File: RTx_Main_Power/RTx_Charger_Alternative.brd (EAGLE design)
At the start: 102.9 x 43.2 mm, 11 parts, among them IC1 TL331, Q1 STW11NM80

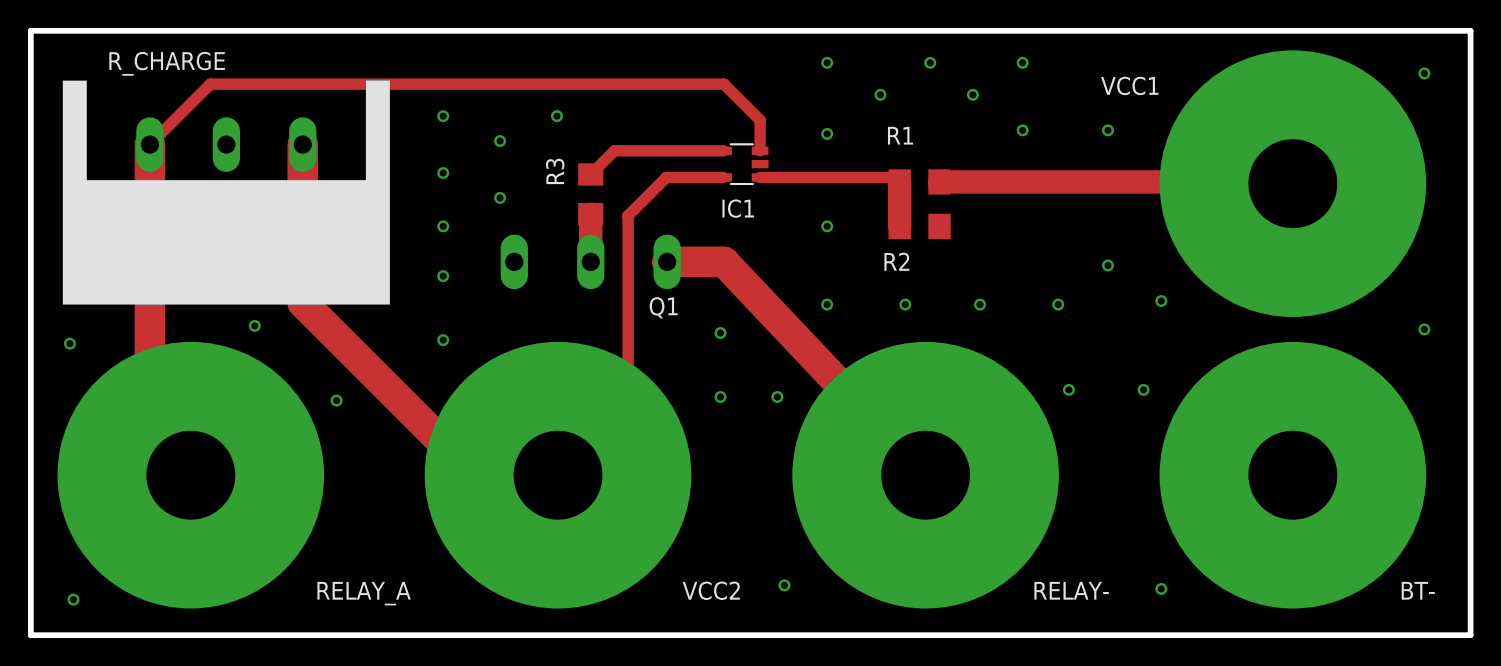
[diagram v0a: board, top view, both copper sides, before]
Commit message: High speed signal routing information added to schematic. Updated Precharge board.
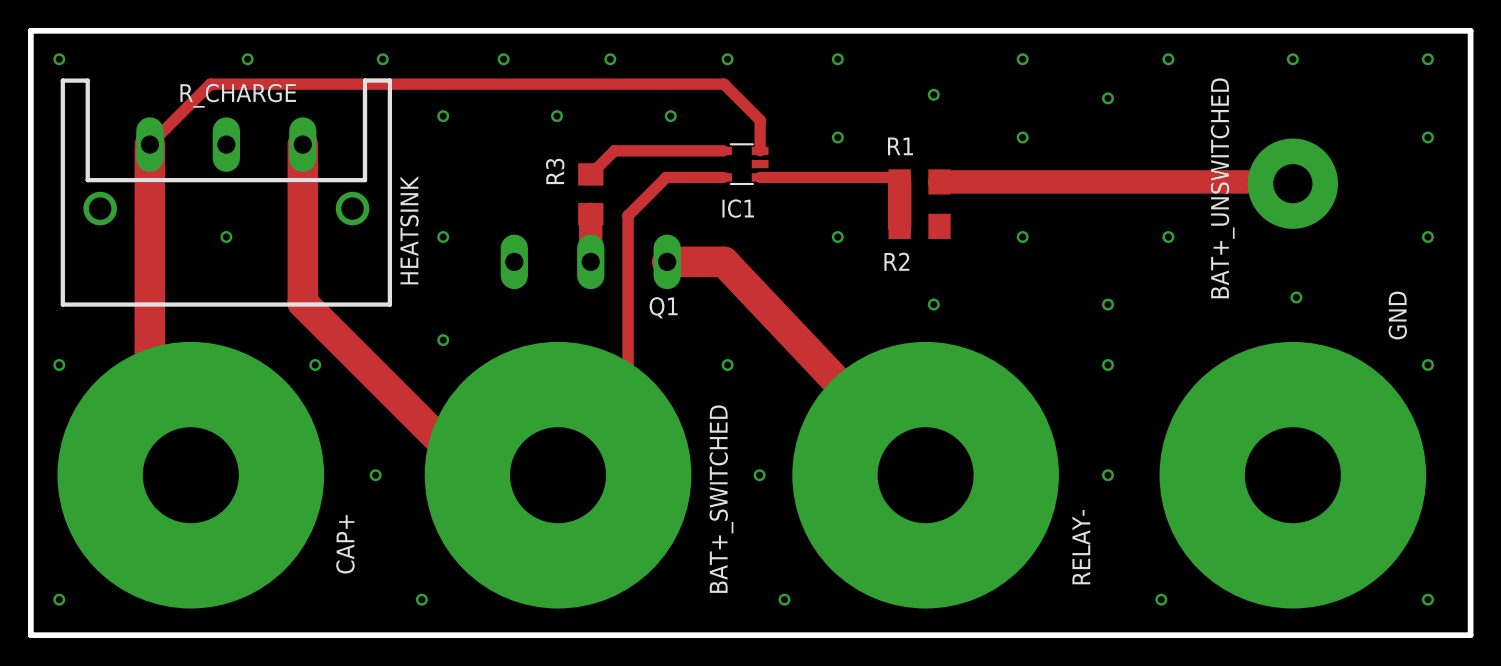
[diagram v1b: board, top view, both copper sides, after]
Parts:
- removed VCC1: TERMINAL, temp_library:TERMINAL_BATTERY
- added BAT+_UNSWITCHED: TERMINAL, temp_library:TERMINAL_RELAY
- added HEATSINK: WA-T247-101E, temp_library:WA-T247-101E
- R_CHARGE: device temp_library:WA-T247-101E -> temp_library:TEH70
- renumbered BT- to GND, RELAY_A to CAP+, VCC2 to BAT+_SWITCHED
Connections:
- net RELAY_A renamed CAP+
- net VCC2 renamed BAT+_SWITCHED
- removed net VCC1: R1.2, VCC1.1
- new net BAT+_UNSWITCHED: BAT+_UNSWITCHED.P$1, R1.2
- net GND: now also HEATSINK.HEATSINK1, HEATSINK.HEATSINK2
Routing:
- net VCC1: track 25.3 -> 0.00 mm
- net BAT+_UNSWITCHED: track 0.00 -> 25.3 mm
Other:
- board text added: "+"
- board text added: "-"
- board text added: "Power Filter Precharge"
- board text added: "RTx"
- board text added: "Robert Corkran Robin Davis Rob Gaskell"
